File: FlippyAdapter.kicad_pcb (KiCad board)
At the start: 2 copper layers, 164.9 x 20.8 mm, 8 parts, among them J1 Conn_02x20_Odd_Even, J2 Conn_02x20_Odd_Even, J3 Board Harness

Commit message: Add libraries submodule
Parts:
- J3: footprint FlippyAdapter:Connector_MegaMax_3000 -> Nieto_Connector:Luminator_MAX3000
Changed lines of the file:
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@@
     )
   )
-  (footprint "FlippyAdapter:Connector_MegaMax_3000" locked (layer "F.Cu")
+  (footprint "Nieto_Connector:Luminator_MAX3000" locked (layer "F.Cu")
     (at 149.6 73.8 90)
     (property "Sheetfile" "FlippyAdapter.kicad_sch")
@@
     )
     (fp_line (start 1.21 40.7) (end 3.87 40.7) (layer "F.SilkS") (width 0.12))
+    (fp_line (start 1.21 -38.1) (end 3.87 -38.1) (layer "F.SilkS") (width 0.12))
     (fp_line (start -3.87 40.7) (end -1.21 40.7) (layer "F.SilkS") (width 0.12))
+    (fp_line (start 3.87 -38.1) (end 3.87 40.7) (layer "F.SilkS") (width 0.12))
+    (fp_line (start -3.87 -38.1) (end -1.21 -38.1) (layer "F.SilkS") (width 0.12))
+    (fp_line (start -3.87 -38.1) (end -3.87 40.7) (layer "F.SilkS") (width 0.12))
+    (fp_line (start -3.87 -39.37) (end -3.87 -40.7) (layer "F.SilkS") (width 0.12))
+    (fp_line (start 1.21 -39.37) (end 1.21 -40.7) (layer "F.SilkS") (width 0.12))
+    (fp_line (start 1.21 -40.7) (end 2.54 -40.7) (layer "F.SilkS") (width 0.12))
     (fp_line (start -3.87 -40.7) (end -2.54 -40.7) (layer "F.SilkS") (width 0.12))
-    (fp_line (start -3.87 -38.1) (end -3.87 40.7) (layer "F.SilkS") (width 0.12))
-    (fp_line (start -3.87 -38.1) (end -1.21 -38.1) (layer "F.SilkS") (width 0.12))
-    (fp_line (start 1.21 -39.37) (end 1.21 -40.7) (layer "F.SilkS") (width 0.12))
+    (fp_line (start -1.21 -38.1) (end -1.21 40.7) (layer "F.SilkS") (width 0.12))
     (fp_line (start 1.21 -38.1) (end 1.21 40.7) (layer "F.SilkS") (width 0.12))
-    (fp_line (start 1.21 -40.7) (end 2.54 -40.7) (layer "F.SilkS") (width 0.12))
-    (fp_line (start 3.87 -38.1) (end 3.87 40.7) (layer "F.SilkS") (width 0.12))
-    (fp_line (start -1.21 -38.1) (end -1.21 40.7) (layer "F.SilkS") (width 0.12))
-    (fp_line (start 1.21 -38.1) (end 3.87 -38.1) (layer "F.SilkS") (width 0.12))
-    (fp_line (start -3.87 -39.37) (end -3.87 -40.7) (layer "F.SilkS") (width 0.12))
+    (fp_line (start -4.34 41.18) (end -0.74 41.18) (layer "F.CrtYd") (width 0.05))
     (fp_line (start -4.34 -41.17) (end -4.34 41.18) (layer "F.CrtYd") (width 0.05))
+    (fp_line (start -0.74 -41.17) (end -4.34 -41.17) (layer "F.CrtYd") (width 0.05))
     (fp_line (start 0.74 -41.17) (end 0.74 41.18) (layer "F.CrtYd") (width 0.05))
+    (fp_line (start 4.34 -41.17) (end 0.74 -41.17) (layer "F.CrtYd") (width 0.05))
+    (fp_line (start -0.74 41.18) (end -0.74 -41.17) (layer "F.CrtYd") (width 0.05))
+    (fp_line (start 0.74 41.18) (end 4.34 41.18) (layer "F.CrtYd") (width 0.05))
     (fp_line (start 4.34 41.18) (end 4.34 -41.17) (layer "F.CrtYd") (width 0.05))
-    (fp_line (start -0.74 -41.17) (end -4.34 -41.17) (layer "F.CrtYd") (width 0.05))
-    (fp_line (start 0.74 41.18) (end 4.34 41.18) (layer "F.CrtYd") (width 0.05))
-    (fp_line (start -0.74 41.18) (end -0.74 -41.17) (layer "F.CrtYd") (width 0.05))
-    (fp_line (start -4.34 41.18) (end -0.74 41.18) (layer "F.CrtYd") (width 0.05))
-    (fp_line (start 4.34 -41.17) (end 0.74 -41.17) (layer "F.CrtYd") (width 0.05))
+    (fp_line (start 1.905 -40.64) (end 3.81 -40.64) (layer "F.Fab") (width 0.1))
+    (fp_line (start -1.27 40.64) (end -3.81 40.64) (layer "F.Fab") (width 0.1))
+    (fp_line (start -3.175 -40.64) (end -1.27 -40.64) (layer "F.Fab") (width 0.1))
+    (fp_line (start 3.81 -40.64) (end 3.81 40.64) (layer "F.Fab") (width 0.1))
+    (fp_line (start 1.27 40.64) (end 1.27 -40.005) (layer "F.Fab") (width 0.1))
+    (fp_line (start -1.27 -40.64) (end -1.27 40.64) (layer "F.Fab") (width 0.1))
     (fp_line (start -3.81 -40.005) (end -3.175 -40.64) (layer "F.Fab") (width 0.1))
-    (fp_line (start 1.27 40.64) (end 1.27 -40.005) (layer "F.Fab") (width 0.1))
-    (fp_line (start 3.81 -40.64) (end 3.81 40.64) (layer "F.Fab") (width 0.1))
+    (fp_line (start 3.81 40.64) (end 1.27 40.64) (layer "F.Fab") (width 0.1))
+    (fp_line (start 1.27 -40.005) (end 1.905 -40.64) (layer "F.Fab") (width 0.1))
     (fp_line (start -3.81 40.64) (end -3.81 -40.005) (layer "F.Fab") (width 0.1))
-    (fp_line (start -1.27 40.64) (end -3.81 40.64) (layer "F.Fab") (width 0.1))
-    (fp_line (start 3.81 40.64) (end 1.27 40.64) (layer "F.Fab") (width 0.1))
-    (fp_line (start 1.905 -40.64) (end 3.81 -40.64) (layer "F.Fab") (width 0.1))
-    (fp_line (start -1.27 -40.64) (end -1.27 40.64) (layer "F.Fab") (width 0.1))
-    (fp_line (start -3.175 -40.64) (end -1.27 -40.64) (layer "F.Fab") (width 0.1))
-    (fp_line (start 1.27 -40.005) (end 1.905 -40.64) (layer "F.Fab") (width 0.1))
     (pad "1" thru_hole rect locked (at -2.54 -39.37 90) (size 1.7 1.7) (drill 1) (layers *.Cu *.Mask)
       (net 61 "PIN_LED-") (pinfunction "Pin_1") (pintype "passive"))
@@
     (pad "64" thru_hole oval locked (at 2.54 39.37 90) (size 1.7 1.7) (drill 1) (layers *.Cu *.Mask)
       (net 53 "COL_27") (pinfunction "Pin_64") (pintype "passive"))
+    (model "${KICAD6_3DMODEL_DIR}/Connector_PinHeader_2.54mm.3dshapes/PinHeader_1x32_P2.54mm_Vertical.step"
+      (offset (xyz 2.5 39.5 -1.5))
+      (scale (xyz 1 1 1))
+      (rotate (xyz 0 180 0))
+    )
+    (model "${KICAD6_3DMODEL_DIR}/Connector_PinHeader_2.54mm.3dshapes/PinHeader_1x32_P2.54mm_Vertical.step"
+      (offset (xyz -2.5 39.5 -1.5))
+      (scale (xyz 1 1 1))
+      (rotate (xyz 0 180 0))
+    )
   )
   (footprint "Symbol:OSHW-Symbol_6.7x6mm_SilkScreen" (layer "F.Cu")

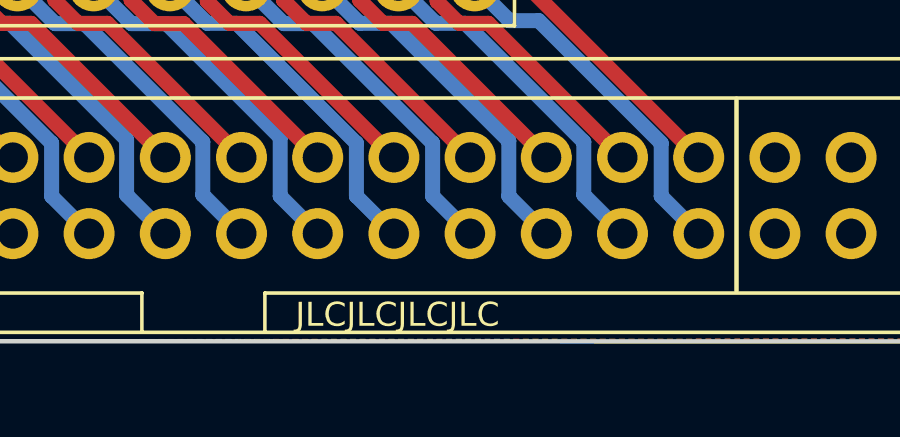
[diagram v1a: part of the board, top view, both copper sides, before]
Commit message: Remove internal library
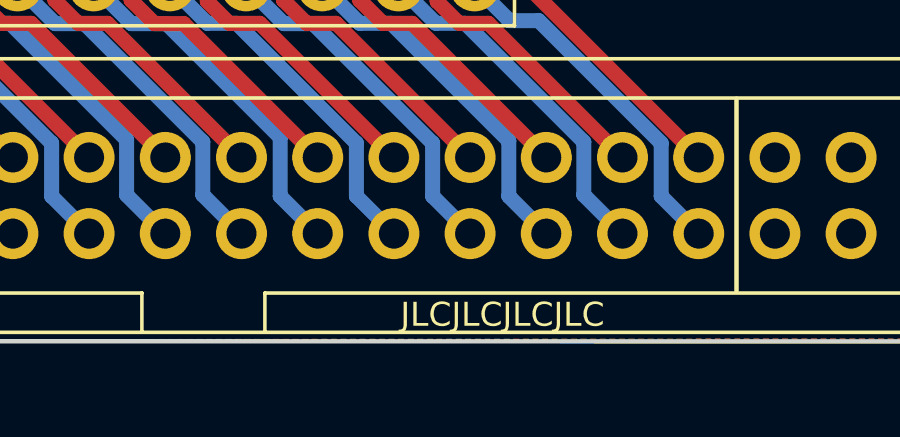
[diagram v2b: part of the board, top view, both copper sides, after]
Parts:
- JLCJLCJLCJLC: footprint FlippyAdapter:JLCJLCJLCJLC -> Nieto_Symbol:JLCPCB_OrderNumber
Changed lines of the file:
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@@
       (net 62 "PIN_GND") (pinfunction "1") (pintype "input"))
   )
-  (footprint "FlippyAdapter:JLCJLCJLCJLC" (layer "F.Cu")
+  (footprint "Nieto_Symbol:JLCPCB_OrderNumber" (layer "F.Cu")
     (at 189.9 87.3)
-    (fp_text reference "JLCJLCJLCJLC" (at -3.5 0 unlocked) (layer "F.SilkS")
+    (attr board_only exclude_from_pos_files exclude_from_bom)
+    (fp_text reference "JLCJLCJLCJLC" (at 0 0 unlocked) (layer "F.SilkS")
       (effects (font (size 0.8 0.8) (thickness 0.15)))
     )
